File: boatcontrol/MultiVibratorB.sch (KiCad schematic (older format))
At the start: 6 parts, among them IC401 CD74HCT221E

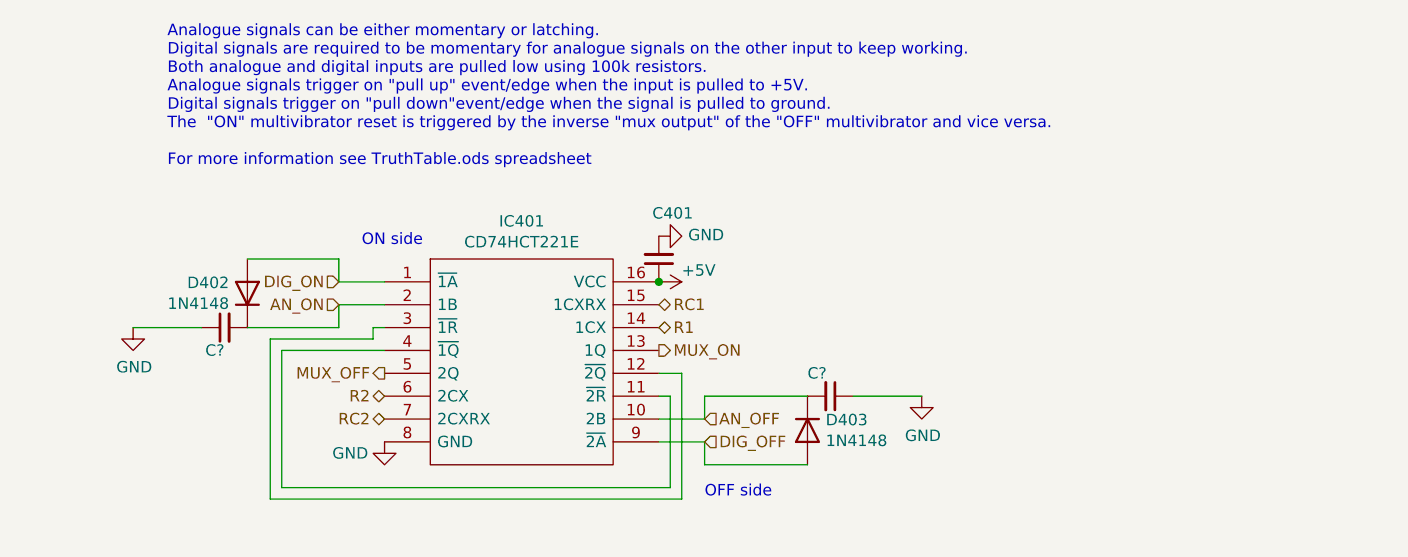
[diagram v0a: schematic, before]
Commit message: Add xors on input
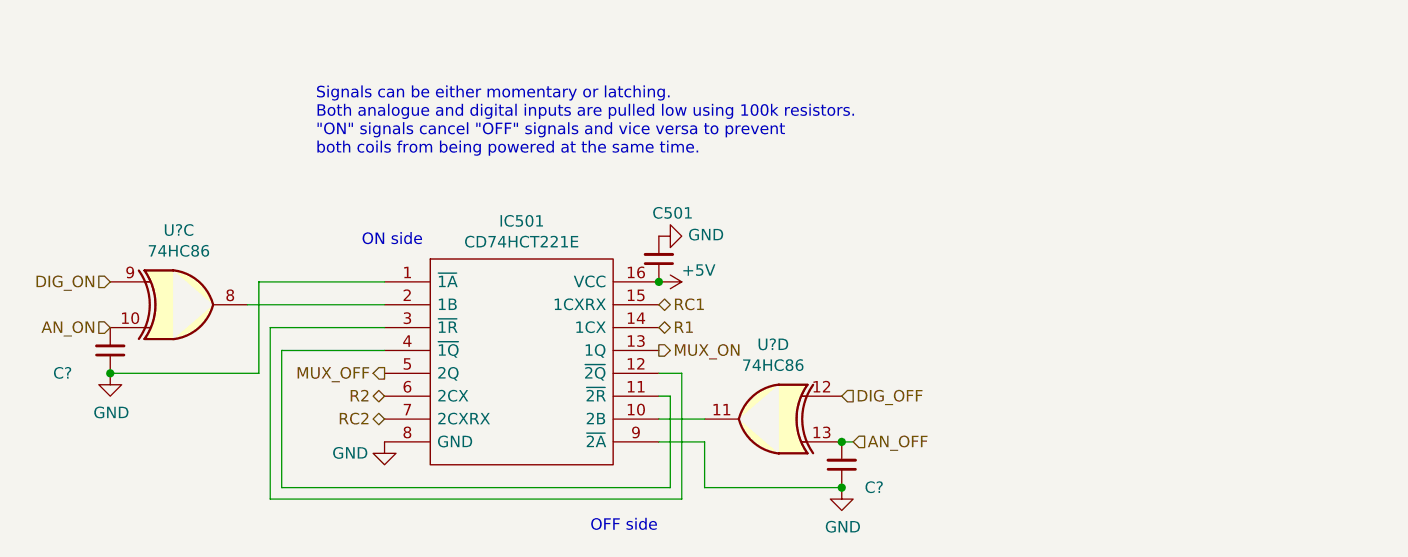
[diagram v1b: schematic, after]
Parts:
- removed D702, D703: 1N4148, Diode_THT:D_DO-35_SOD27_P7.62mm_Horizontal, symbol Diode:1N4148
- added U? (x2): 74HC86, symbol 74xx:74HC86
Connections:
- net AN_OFF: now also U?.13; no longer IC401.10 (2B)
- net AN_ON: now also U?.10; no longer IC401.2 (1B)
- net DIG_OFF: now also U?.12; no longer IC401.9 (~2A)
- net DIG_ON: now also U?.9; no longer IC401.1 (~1A)
- net GND: now also IC401.1 (~1A), IC401.9 (~2A)
- new net: IC401.10 (2B), U?.11
- new net: IC401.2 (1B), U?.8
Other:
- note added: "Signals can be either momentary or latching.\nBoth analogue and digital inputs are pulled low using 100k resistors.\n"ON" signals cancel "OFF" signals and vice versa to prevent\nboth coils from being powered at the same time."
- note removed: "Analogue signals can be either momentary or latching.\nDigital signals are required to be momentary for analogue signals on the other input to keep working.\nBoth analogue and digital inputs are pulled low using 100k resistors.\nAnalogue signals trigger on "pull up" event/edge when the input is pulled to +5V.\nDigital signals trigger on "pull down"event/edge when the signal is pulled to ground.\n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"
- moved on the sheet: C?

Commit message: Top
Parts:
- gave numbers to parts that had none: 3

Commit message: Renamed
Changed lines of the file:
@@
 $Descr A4 11693 8268
 encoding utf-8
-Sheet 35 97
+Sheet 57 97
 Title "Boat Control Hat"
 Date ""
@@
 AR Path="/D1BB8DB4/5F75E923/604747F3/5FD2B9DE" Ref="IC7301"  Part="1"
 AR Path="/D1BB8DB4/5F75E923/604747FF/5FD2B9DE" Ref="IC7401"  Part="1"
-F 0 "IC3401" H 5450 4215 50  0000 C CNN
+F 0 "IC6501" H 5450 4215 50  0000 C CNN
 F 1 "CD74HCT221E" H 5450 4124 50  0000 C CNN
 F 2 "DIP794W53P254L1930H508Q16N" H 5900 4050 50  0001 L CNN
@@
 AR Path="/D1BB8DB4/5F75E923/604747F3/60314A0F" Ref="#PWR07302"  Part="1"
 AR Path="/D1BB8DB4/5F75E923/604747FF/60314A0F" Ref="#PWR07402"  Part="1"
-F 0 "#PWR03402" H 4850 4400 50  0001 C CNN
+F 0 "#PWR06502" H 4850 4400 50  0001 C CNN
 F 1 "GND" H 4700 4600 50  0000 C CNN
 F 2 "" H 4850 4650 50  0001 C CNN
@@
 AR Path="/D1BB8DB4/5F75E923/604747F3/5FD9FC74" Ref="#PWR07301"  Part="1"
 AR Path="/D1BB8DB4/5F75E923/604747FF/5FD9FC74" Ref="#PWR07401"  Part="1"
-F 0 "#PWR03401" H 6050 3800 50  0001 C CNN
+F 0 "#PWR06501" H 6050 3800 50  0001 C CNN
 F 1 "+5V" V 6000 4050 50  0000 L CNN
 F 2 "" H 6050 3950 50  0001 C CNN
@@
 AR Path="/D1BB8DB4/5F317CB5/60365B0F/61CAF5C8" Ref="#PWR0183"  Part="1"
 AR Path="/D1BB8DB4/5F317CB5/60365B35/61CAF5C8" Ref="#PWR0185"  Part="1"
-F 0 "#PWR0170" H 6050 3500 50  0001 C CNN
+F 0 "#PWR0178" H 6050 3500 50  0001 C CNN
 F 1 "GND" V 6055 3622 50  0000 R CNN
 F 2 "" H 6050 3750 50  0001 C CNN
@@
 AR Path="/D1BB8DB4/5F317CB5/60365B0F/61CAE2AB" Ref="C8001"  Part="1"
 AR Path="/D1BB8DB4/5F317CB5/60365B35/61CAE2AB" Ref="C8201"  Part="1"
-F 0 "C3401" H 5900 3650 50  0000 L CNN
+F 0 "C6501" H 5900 3650 50  0000 L CNN
 F 1 "0.1μF" H 6141 3805 50  0001 L CNN
 F 2 "Capacitor_THT:C_Disc_D7.5mm_W5.0mm_P5.00mm" H 6050 3850 50  0001 C CNN
@@
 AR Path="/D1BB8DB4/5F317CB5/60365B29/602120C6" Ref="C6902"  Part="1"
 AR Path="/D1BB8DB4/5F317CB5/60365B41/602120C6" Ref="C7103"  Part="1"
-F 0 "C3502" H 6950 4850 50  0000 L CNN
+F 0 "C5702" H 6950 4850 50  0000 L CNN
 F 1 "1µF" H 6000 4650 50  0001 L CNN
 F 2 "Capacitor_THT:C_Disc_D7.5mm_W5.0mm_P5.00mm" H 6850 4750 50  0001 C CNN
@@
 AR Path="/D1BB8DB4/5F317CB5/60365B29/60314A11" Ref="#PWR0350"  Part="1"
 AR Path="/D1BB8DB4/5F317CB5/60365B41/60314A11" Ref="#PWR0354"  Part="1"
-F 0 "#PWR0293" H 6850 4600 50  0001 C CNN
+F 0 "#PWR0328" H 6850 4600 50  0001 C CNN
 F 1 "GND" H 6855 4677 50  0000 C CNN
 F 2 "" H 6850 4850 50  0001 C CNN
@@
 AR Path="/D1BB8DB4/5F317CB5/60365B29/60216860" Ref="#PWR0351"  Part="1"
 AR Path="/D1BB8DB4/5F317CB5/60365B41/60216860" Ref="#PWR0355"  Part="1"
-F 0 "#PWR0294" H 3650 4100 50  0001 C CNN
+F 0 "#PWR0329" H 3650 4100 50  0001 C CNN
 F 1 "GND" H 3655 4177 50  0000 C CNN
 F 2 "" H 3650 4350 50  0001 C CNN
@@
 AR Path="/D1BB8DB4/5F317CB5/60365B29/6021685A" Ref="C6901"  Part="1"
 AR Path="/D1BB8DB4/5F317CB5/60365B41/6021685A" Ref="C7102"  Part="1"
-F 0 "C3501" H 3400 4350 50  0000 L CNN
+F 0 "C5701" H 3400 4350 50  0000 L CNN
 F 1 "1µF" H 2800 4150 50  0001 L CNN
 F 2 "Capacitor_THT:C_Disc_D7.5mm_W5.0mm_P5.00mm" H 3650 4250 50  0001 C CNN
@@
 AR Path="/D1BB8DB4/5F746103/60365B29/604BDC57" Ref="U4002"  Part="3"
 AR Path="/D1BB8DB4/5F746103/60365B41/604BDC57" Ref="U4003"  Part="3"
-AR Path="/D1BB8DB4/5F76AF55/604747E7/604BDC57" Ref="U5001"  Part="3"
-AR Path="/D1BB8DB4/5F76AF55/604747FF/604BDC57" Ref="U5601"  Part="3"
-AR Path="/D1BB8DB4/5F75E923/604747E7/604BDC57" Ref="U5901"  Part="3"
-AR Path="/D1BB8DB4/5F75E923/604747FF/604BDC57" Ref="U6501"  Part="3"
-AR Path="/D1BB8DB4/5F317CB5/60365B29/604BDC57" Ref="U6801"  Part="3"
-AR Path="/D1BB8DB4/5F317CB5/60365B41/604BDC57" Ref="U7002"  Part="3"
-F 0 "U3003" H 3950 4375 50  0000 C CNN
+AR Path="/D1BB8DB4/5F76AF55/604747E7/604BDC57" Ref="U6102"  Part="3"
+AR Path="/D1BB8DB4/5F76AF55/604747FF/604BDC57" Ref="U6103"  Part="3"
+AR Path="/D1BB8DB4/5F75E923/604747E7/604BDC57" Ref="U7002"  Part="3"
+AR Path="/D1BB8DB4/5F75E923/604747FF/604BDC57" Ref="U7003"  Part="3"
+AR Path="/D1BB8DB4/5F317CB5/60365B29/604BDC57" Ref="U7902"  Part="3"
+AR Path="/D1BB8DB4/5F317CB5/60365B41/604BDC57" Ref="U7903"  Part="3"
+F 0 "U6103" H 3950 4375 50  0000 C CNN
 F 1 "74HC86" H 3950 4284 50  0000 C CNN
 F 2 "" H 3950 4050 50  0001 C CNN
@@
 AR Path="/D1BB8DB4/5F746103/60365B29/604BF9DE" Ref="U4002"  Part="4"
 AR Path="/D1BB8DB4/5F746103/60365B41/604BF9DE" Ref="U4003"  Part="4"
-AR Path="/D1BB8DB4/5F76AF55/604747E7/604BF9DE" Ref="U5001"  Part="4"
-AR Path="/D1BB8DB4/5F76AF55/604747FF/604BF9DE" Ref="U5601"  Part="4"
-AR Path="/D1BB8DB4/5F75E923/604747E7/604BF9DE" Ref="U5901"  Part="4"
-AR Path="/D1BB8DB4/5F75E923/604747FF/604BF9DE" Ref="U6501"  Part="4"
-AR Path="/D1BB8DB4/5F317CB5/60365B29/604BF9DE" Ref="U6801"  Part="4"
-AR Path="/D1BB8DB4/5F317CB5/60365B41/604BF9DE" Ref="U7002"  Part="4"
-F 0 "U3003" H 6550 4875 50  0000 C CNN
-F 1 "74HC86" H 6550 4784 50  0000 C CNN
+AR Path="/D1BB8DB4/5F76AF55/604747E7/604BF9DE" Ref="U6102"  Part="4"
+AR Path="/D1BB8DB4/5F76AF55/604747FF/604BF9DE" Ref="U6103"  Part="4"
+AR Path="/D1BB8DB4/5F75E923/604747E7/604BF9DE" Ref="U7002"  Part="4"
+AR Path="/D1BB8DB4/5F75E923/604747FF/604BF9DE" Ref="U7003"  Part="4"
+AR Path="/D1BB8DB4/5F317CB5/60365B29/604BF9DE" Ref="U7902"  Part="4"
+AR Path="/D1BB8DB4/5F317CB5/60365B41/604BF9DE" Ref="U7903"  Part="4"
+F 0 "U6103" H 6450 4900 50  0000 C CNN
+F 1 "74HC86" H 6450 4800 50  0000 C CNN
 F 2 "" H 6550 4550 50  0001 C CNN
 F 3 "http://www.ti.com/lit/gpn/sn74HC86" H 6550 4550 50  0001 C CNN

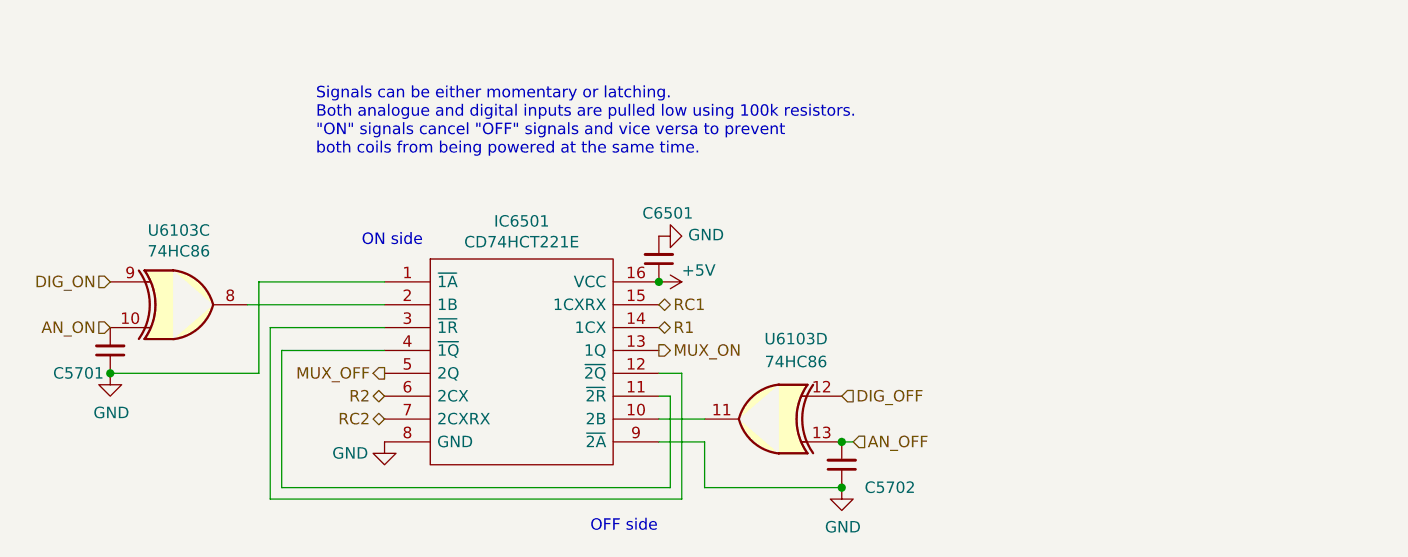
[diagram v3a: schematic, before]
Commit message: Update cap numbering
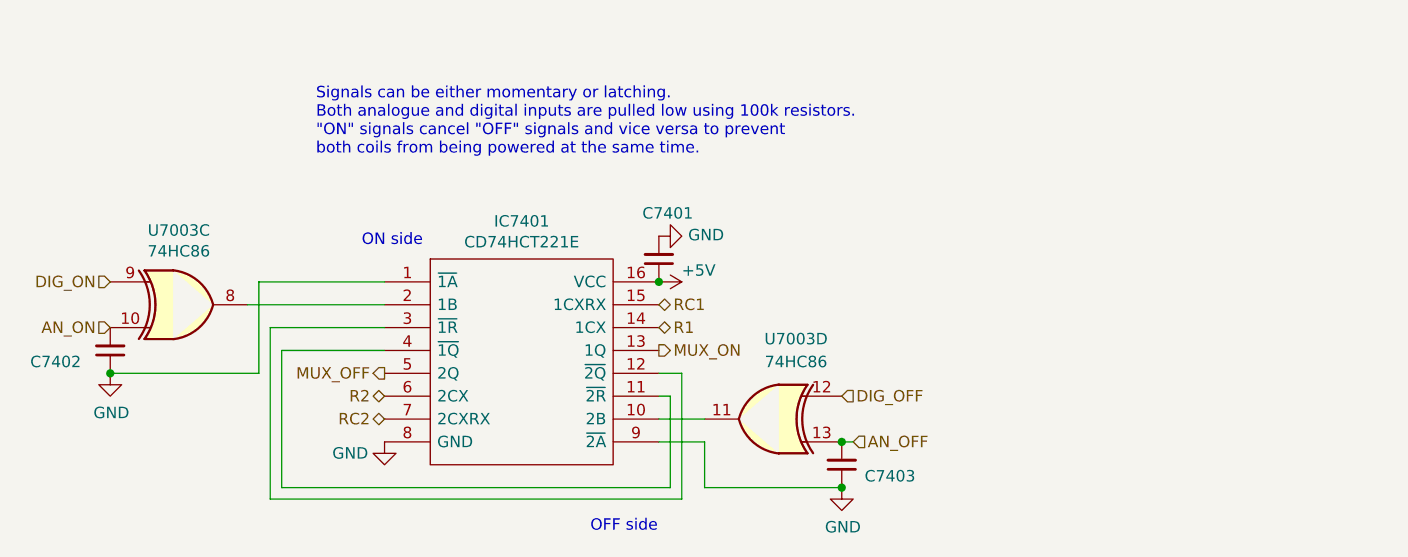
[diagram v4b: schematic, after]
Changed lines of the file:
@@
 $Descr A4 11693 8268
 encoding utf-8
-Sheet 57 97
+Sheet 66 97
 Title "Boat Control Hat"
 Date ""
@@
 AR Path="/D1BB8DB4/5F75E923/604747F3/5FD2B9DE" Ref="IC7301"  Part="1"
 AR Path="/D1BB8DB4/5F75E923/604747FF/5FD2B9DE" Ref="IC7401"  Part="1"
-F 0 "IC6501" H 5450 4215 50  0000 C CNN
+F 0 "IC7401" H 5450 4215 50  0000 C CNN
 F 1 "CD74HCT221E" H 5450 4124 50  0000 C CNN
 F 2 "DIP794W53P254L1930H508Q16N" H 5900 4050 50  0001 L CNN
@@
 AR Path="/D1BB8DB4/5F75E923/604747F3/60314A0F" Ref="#PWR07302"  Part="1"
 AR Path="/D1BB8DB4/5F75E923/604747FF/60314A0F" Ref="#PWR07402"  Part="1"
-F 0 "#PWR06502" H 4850 4400 50  0001 C CNN
+F 0 "#PWR07402" H 4850 4400 50  0001 C CNN
 F 1 "GND" H 4700 4600 50  0000 C CNN
 F 2 "" H 4850 4650 50  0001 C CNN
@@
 AR Path="/D1BB8DB4/5F75E923/604747F3/5FD9FC74" Ref="#PWR07301"  Part="1"
 AR Path="/D1BB8DB4/5F75E923/604747FF/5FD9FC74" Ref="#PWR07401"  Part="1"
-F 0 "#PWR06501" H 6050 3800 50  0001 C CNN
+F 0 "#PWR07401" H 6050 3800 50  0001 C CNN
 F 1 "+5V" V 6000 4050 50  0000 L CNN
 F 2 "" H 6050 3950 50  0001 C CNN
@@
 AR Path="/D1BB8DB4/5F317CB5/60365B0F/61CAF5C8" Ref="#PWR0183"  Part="1"
 AR Path="/D1BB8DB4/5F317CB5/60365B35/61CAF5C8" Ref="#PWR0185"  Part="1"
-F 0 "#PWR0178" H 6050 3500 50  0001 C CNN
+F 0 "#PWR0182" H 6050 3500 50  0001 C CNN
 F 1 "GND" V 6055 3622 50  0000 R CNN
 F 2 "" H 6050 3750 50  0001 C CNN
@@
 AR Path="/D1BB8DB4/5F317CB5/60365B0F/61CAE2AB" Ref="C8001"  Part="1"
 AR Path="/D1BB8DB4/5F317CB5/60365B35/61CAE2AB" Ref="C8201"  Part="1"
-F 0 "C6501" H 5900 3650 50  0000 L CNN
+F 0 "C7401" H 5900 3650 50  0000 L CNN
 F 1 "0.1μF" H 6141 3805 50  0001 L CNN
 F 2 "Capacitor_THT:C_Disc_D7.5mm_W5.0mm_P5.00mm" H 6050 3850 50  0001 C CNN
@@
 AR Path="/D16552B4/5FA17F6C/61B577C5/602120C6" Ref="C2902"  Part="1"
 AR Path="/D16552B4/5FA17F86/61B95A95/602120C6" Ref="C3502"  Part="1"
-AR Path="/D1BB8DB4/5F746103/60365B29/602120C6" Ref="C4202"  Part="1"
-AR Path="/D1BB8DB4/5F746103/60365B41/602120C6" Ref="C4402"  Part="1"
-AR Path="/D1BB8DB4/5F76AF55/604747E7/602120C6" Ref="C5106"  Part="1"
-AR Path="/D1BB8DB4/5F76AF55/604747FF/602120C6" Ref="C5702"  Part="1"
-AR Path="/D1BB8DB4/5F75E923/604747E7/602120C6" Ref="C6002"  Part="1"
-AR Path="/D1BB8DB4/5F75E923/604747FF/602120C6" Ref="C6602"  Part="1"
-AR Path="/D1BB8DB4/5F317CB5/60365B29/602120C6" Ref="C6902"  Part="1"
-AR Path="/D1BB8DB4/5F317CB5/60365B41/602120C6" Ref="C7103"  Part="1"
-F 0 "C5702" H 6950 4850 50  0000 L CNN
+AR Path="/D1BB8DB4/5F746103/60365B29/602120C6" Ref="C5403"  Part="1"
+AR Path="/D1BB8DB4/5F746103/60365B41/602120C6" Ref="C5603"  Part="1"
+AR Path="/D1BB8DB4/5F76AF55/604747E7/602120C6" Ref="C6303"  Part="1"
+AR Path="/D1BB8DB4/5F76AF55/604747FF/602120C6" Ref="C6503"  Part="1"
+AR Path="/D1BB8DB4/5F75E923/604747E7/602120C6" Ref="C7203"  Part="1"
+AR Path="/D1BB8DB4/5F75E923/604747FF/602120C6" Ref="C7403"  Part="1"
+AR Path="/D1BB8DB4/5F317CB5/60365B29/602120C6" Ref="C8103"  Part="1"
+AR Path="/D1BB8DB4/5F317CB5/60365B41/602120C6" Ref="C8303"  Part="1"
+F 0 "C7403" H 6950 4800 50  0000 L CNN
 F 1 "1µF" H 6000 4650 50  0001 L CNN
 F 2 "Capacitor_THT:C_Disc_D7.5mm_W5.0mm_P5.00mm" H 6850 4750 50  0001 C CNN
@@
 AR Path="/D1BB8DB4/5F317CB5/60365B29/60314A11" Ref="#PWR0350"  Part="1"
 AR Path="/D1BB8DB4/5F317CB5/60365B41/60314A11" Ref="#PWR0354"  Part="1"
-F 0 "#PWR0328" H 6850 4600 50  0001 C CNN
+F 0 "#PWR0339" H 6850 4600 50  0001 C CNN
 F 1 "GND" H 6855 4677 50  0000 C CNN
 F 2 "" H 6850 4850 50  0001 C CNN
@@
 AR Path="/D1BB8DB4/5F317CB5/60365B29/60216860" Ref="#PWR0351"  Part="1"
 AR Path="/D1BB8DB4/5F317CB5/60365B41/60216860" Ref="#PWR0355"  Part="1"
-F 0 "#PWR0329" H 3650 4100 50  0001 C CNN
+F 0 "#PWR0340" H 3650 4100 50  0001 C CNN
 F 1 "GND" H 3655 4177 50  0000 C CNN
 F 2 "" H 3650 4350 50  0001 C CNN
@@
 AR Path="/D16552B4/5FA17F6C/61B577C5/6021685A" Ref="C2901"  Part="1"
 AR Path="/D16552B4/5FA17F86/61B95A95/6021685A" Ref="C3501"  Part="1"
-AR Path="/D1BB8DB4/5F746103/60365B29/6021685A" Ref="C4201"  Part="1"
-AR Path="/D1BB8DB4/5F746103/60365B41/6021685A" Ref="C4401"  Part="1"
-AR Path="/D1BB8DB4/5F76AF55/604747E7/6021685A" Ref="C5105"  Part="1"
-AR Path="/D1BB8DB4/5F76AF55/604747FF/6021685A" Ref="C5701"  Part="1"
-AR Path="/D1BB8DB4/5F75E923/604747E7/6021685A" Ref="C6001"  Part="1"
-AR Path="/D1BB8DB4/5F75E923/604747FF/6021685A" Ref="C6601"  Part="1"
-AR Path="/D1BB8DB4/5F317CB5/60365B29/6021685A" Ref="C6901"  Part="1"
-AR Path="/D1BB8DB4/5F317CB5/60365B41/6021685A" Ref="C7102"  Part="1"
-F 0 "C5701" H 3400 4350 50  0000 L CNN
+AR Path="/D1BB8DB4/5F746103/60365B29/6021685A" Ref="C5402"  Part="1"
+AR Path="/D1BB8DB4/5F746103/60365B41/6021685A" Ref="C5602"  Part="1"
+AR Path="/D1BB8DB4/5F76AF55/604747E7/6021685A" Ref="C6302"  Part="1"
+AR Path="/D1BB8DB4/5F76AF55/604747FF/6021685A" Ref="C6502"  Part="1"
+AR Path="/D1BB8DB4/5F75E923/604747E7/6021685A" Ref="C7202"  Part="1"
+AR Path="/D1BB8DB4/5F75E923/604747FF/6021685A" Ref="C7402"  Part="1"
+AR Path="/D1BB8DB4/5F317CB5/60365B29/6021685A" Ref="C8102"  Part="1"
+AR Path="/D1BB8DB4/5F317CB5/60365B41/6021685A" Ref="C8302"  Part="1"
+F 0 "C7402" H 3300 4300 50  0000 L CNN
 F 1 "1µF" H 2800 4150 50  0001 L CNN
 F 2 "Capacitor_THT:C_Disc_D7.5mm_W5.0mm_P5.00mm" H 3650 4250 50  0001 C CNN
@@
 AR Path="/D1BB8DB4/5F317CB5/60365B29/604BDC57" Ref="U7902"  Part="3"
 AR Path="/D1BB8DB4/5F317CB5/60365B41/604BDC57" Ref="U7903"  Part="3"
-F 0 "U6103" H 3950 4375 50  0000 C CNN
+F 0 "U7003" H 3950 4375 50  0000 C CNN
 F 1 "74HC86" H 3950 4284 50  0000 C CNN
 F 2 "" H 3950 4050 50  0001 C CNN
@@
 AR Path="/D1BB8DB4/5F317CB5/60365B29/604BF9DE" Ref="U7902"  Part="4"
 AR Path="/D1BB8DB4/5F317CB5/60365B41/604BF9DE" Ref="U7903"  Part="4"
-F 0 "U6103" H 6450 4900 50  0000 C CNN
+F 0 "U7003" H 6450 4900 50  0000 C CNN
 F 1 "74HC86" H 6450 4800 50  0000 C CNN
 F 2 "" H 6550 4550 50  0001 C CNN
